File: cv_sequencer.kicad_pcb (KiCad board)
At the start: 4 copper layers, 111.3 x 22.4 mm, 106 parts, among them J1 :MIDI_IO, J10 PJ398SM, J11 PJ398SM, J12 PJ398SM, J13 PJ398SM, J2 SWD, J3 3086_Connector_Eurorack_Power, J4 3096_USBC_RA_SMD, J5 CV_OFFSET, J6 PJ398SM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

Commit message: Started firmware. Didn't realize RP2040 needed external flash. But luckily found linker script that can load and execute code straight from RAM
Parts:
- U1: value 3097_TFT_Display_SPI -> 3097_TFT+SD_1.14in

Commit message: Changes from a while ago
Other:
- board text added: "Notes from testing - For REV 0.2"
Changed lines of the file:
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@@
       (connect_pads (clearance 0))
       (min_thickness 0.254)
-      (keepout (tracks not_allowed) (vias not_allowed) (pads not_allowed ) (copperpour not_allowed) (footprints not_allowed))
+      (keepout (tracks not_allowed) (vias not_allowed) (pads not_allowed) (copperpour not_allowed) (footprints not_allowed))
       (fill (thermal_gap 0.508) (thermal_bridge_width 0.508))
       (polygon
@@
       (connect_pads (clearance 0))
       (min_thickness 0.254)
-      (keepout (tracks not_allowed) (vias not_allowed) (pads not_allowed ) (copperpour not_allowed) (footprints not_allowed))
+      (keepout (tracks not_allowed) (vias not_allowed) (pads not_allowed) (copperpour not_allowed) (footprints not_allowed))
       (fill (thermal_gap 0.508) (thermal_bridge_width 0.508))
       (polygon
@@
       (connect_pads (clearance 0))
       (min_thickness 0.254)
-      (keepout (tracks not_allowed) (vias not_allowed) (pads not_allowed ) (copperpour not_allowed) (footprints not_allowed))
+      (keepout (tracks not_allowed) (vias not_allowed) (pads not_allowed) (copperpour not_allowed) (footprints not_allowed))
       (fill (thermal_gap 0.508) (thermal_bridge_width 0.508))
       (polygon
@@
       (connect_pads (clearance 0))
       (min_thickness 0.254)
-      (keepout (tracks not_allowed) (vias not_allowed) (pads not_allowed ) (copperpour not_allowed) (footprints not_allowed))
+      (keepout (tracks not_allowed) (vias not_allowed) (pads not_allowed) (copperpour not_allowed) (footprints not_allowed))
       (fill (thermal_gap 0.508) (thermal_bridge_width 0.508))
       (polygon
@@
       (connect_pads (clearance 0))
       (min_thickness 0.254)
-      (keepout (tracks not_allowed) (vias not_allowed) (pads not_allowed ) (copperpour not_allowed) (footprints not_allowed))
+      (keepout (tracks not_allowed) (vias not_allowed) (pads not_allowed) (copperpour not_allowed) (footprints not_allowed))
       (fill (thermal_gap 0.508) (thermal_bridge_width 0.508))
       (polygon
@@
       (connect_pads (clearance 0))
       (min_thickness 0.254)
-      (keepout (tracks not_allowed) (vias not_allowed) (pads not_allowed ) (copperpour not_allowed) (footprints not_allowed))
+      (keepout (tracks not_allowed) (vias not_allowed) (pads not_allowed) (copperpour not_allowed) (footprints not_allowed))
       (fill (thermal_gap 0.508) (thermal_bridge_width 0.508))
       (polygon
@@
       (connect_pads (clearance 0))
       (min_thickness 0.254)
-      (keepout (tracks not_allowed) (vias not_allowed) (pads not_allowed ) (copperpour not_allowed) (footprints not_allowed))
+      (keepout (tracks not_allowed) (vias not_allowed) (pads not_allowed) (copperpour not_allowed) (footprints not_allowed))
       (fill (thermal_gap 0.508) (thermal_bridge_width 0.508))
       (polygon
@@
       (connect_pads (clearance 0))
       (min_thickness 0.254)
-      (keepout (tracks not_allowed) (vias not_allowed) (pads not_allowed ) (copperpour not_allowed) (footprints not_allowed))
+      (keepout (tracks not_allowed) (vias not_allowed) (pads not_allowed) (copperpour not_allowed) (footprints not_allowed))
       (fill (thermal_gap 0.508) (thermal_bridge_width 0.508))
       (polygon
@@
     (fp_line (start -2.044 -1.172) (end -1.544 -1.672) (layer "B.Fab") (width 0.1))
     (fp_arc (start -0.844 1.027999) (mid -1.404147 -0.072) (end -0.844 -1.171999) (layer "B.Fab") (width 0.1))
-    (fp_arc (start 0.855999 -1.171999) (mid 1.45984 -0.072) (end 0.856 1.027999) (layer "B.Fab") (width 0.1))
+    (fp_arc (start 0.855999 -1.171999) (mid 1.459839 -0.072) (end 0.856 1.027999) (layer "B.Fab") (width 0.1))
     (pad "1" smd rect (at -2.019 1.003) (size 1.05 0.65) (layers "B.Cu" "B.Paste" "B.Mask")
       (net 2 "GND") (pinfunction "1") (pintype "passive"))
@@
     (fp_line (start -2.044 1.528) (end 2.156 1.528) (layer "B.Fab") (width 0.1))
     (fp_arc (start -0.844 1.027999) (mid -1.404147 -0.072) (end -0.844 -1.171999) (layer "B.Fab") (width 0.1))
-    (fp_arc (start 0.855999 -1.171999) (mid 1.45984 -0.072) (end 0.856 1.027999) (layer "B.Fab") (width 0.1))
+    (fp_arc (start 0.855999 -1.171999) (mid 1.459839 -0.072) (end 0.856 1.027999) (layer "B.Fab") (width 0.1))
     (pad "1" smd rect (at 2.131 1.003 180) (size 1.05 0.65) (layers "B.Cu" "B.Paste" "B.Mask")
       (net 16 "/~{RESET}") (pinfunction "1") (pintype "passive"))
@@
     (effects (font (size 1.016 1.016) (thickness 0.1524) italic) (justify mirror))
   )
+  (gr_text "Notes from testing - For REV 0.2" (at 71.12 64.008) (layer "Cmts.User")
+    (effects (font (size 1 1) (thickness 0.15)))
+  )
   (gr_text "CV Sequencer Eurorack Module\n1U, 22HP" (at 72.009 46.736) (layer "Cmts.User")
     (effects (font (size 2.032 2.032) (thickness 0.3048)))
@@
     (height -3.8608)
     (orientation 0)
-    (gr_text "4380.0000 mils" (at 162.306 60.4012) (layer "F.Fab")
+    (gr_text "111.2520 mm" (at 162.306 60.4012) (layer "F.Fab")
       (effects (font (size 1.524 1.524) (thickness 0.3048)))
     )

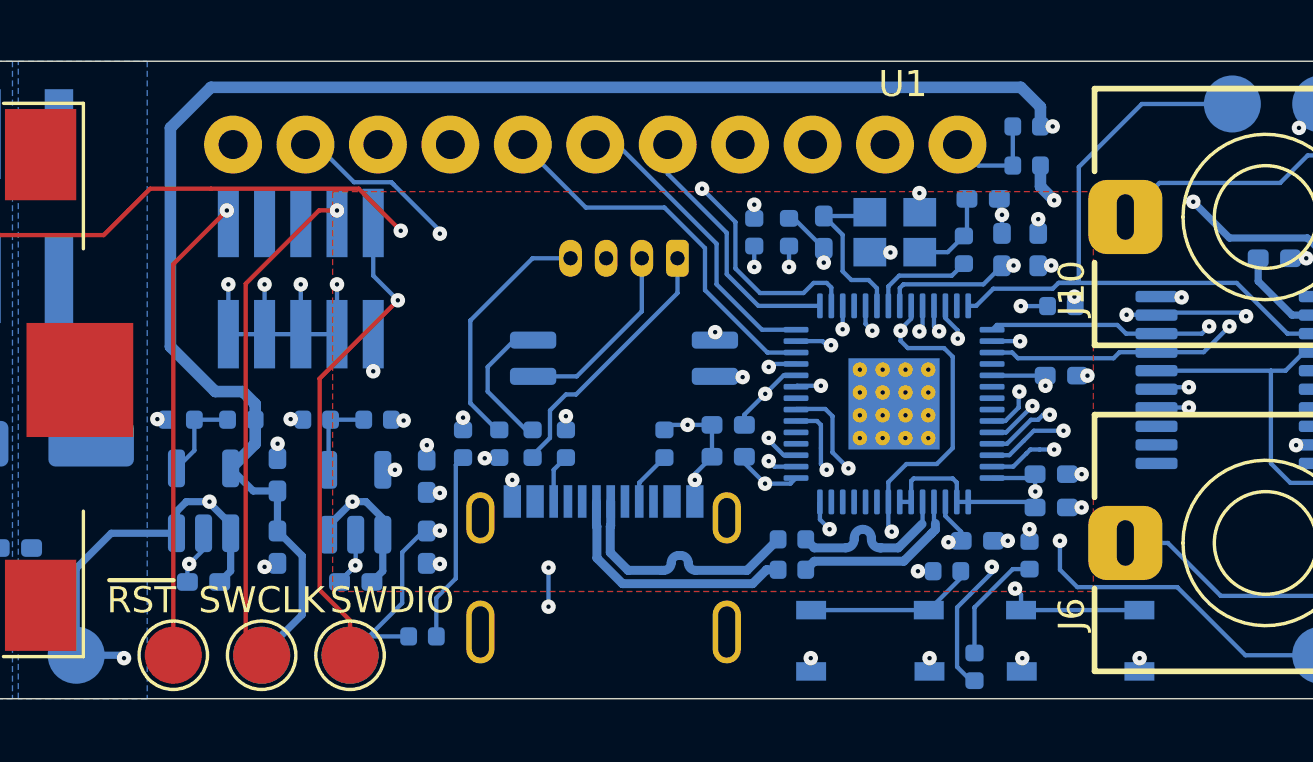
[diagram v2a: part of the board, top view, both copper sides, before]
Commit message: Routed Flash chip.. need to figure out second set of USB lines
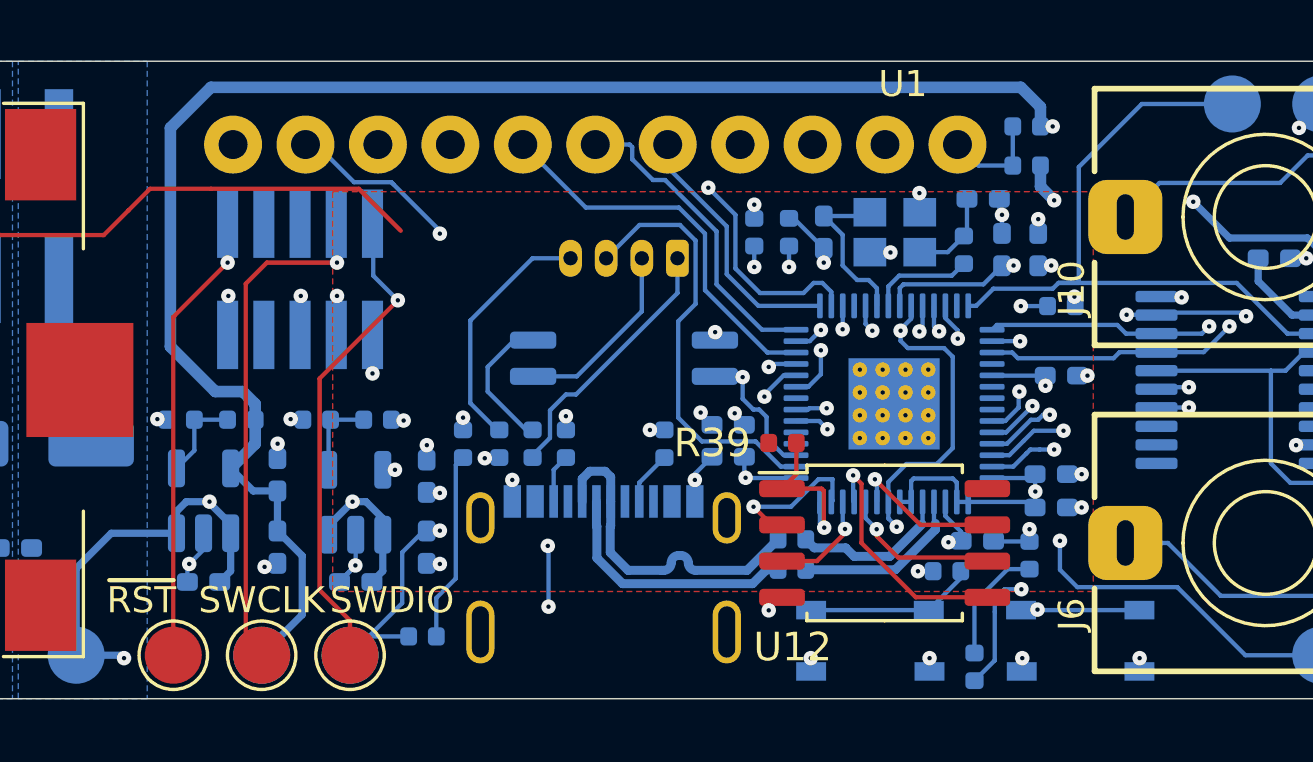
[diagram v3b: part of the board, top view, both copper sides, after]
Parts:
- added R39: 4008_Resistor_SMD_10k_0.125W_1%, Shulltronics_Generics:RES-0402, F.Cu at (146.3, 77.9)
- added U12: 4048_W25Q16JVSSIQ, Shulltronics_Integrated_Circuits:4048_16Mb_Flash_SOIC8, F.Cu at (149.9, 81.9)
- J10, J11, J12, J13, J6, J7, J8, J9: value PJ398SM -> 3085_MiniJack_Thonk_Vert
- J2: value SWD -> 4005_SWD_Header
- U1: value 3097_TFT+SD_1.14in -> 3097_TFT_Display_SPI
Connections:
- net Net-(R5-Pad1) renamed /QSPI_CS
- J2 pad 7: GND -> unconnected-(J2-Pad7)
- J4 pad B6: unconnected-(J4-PadB6) -> /USB_D+
- J4 pad B7: unconnected-(J4-PadB7) -> /USB_D-
- U2 pad 51: unconnected-(U2-Pad51) -> /QSPI_DATA3
- U2 pad 52: unconnected-(U2-Pad52) -> /QSPI_SCK
- U2 pad 53: unconnected-(U2-Pad53) -> /QSPI_DATA0
- U2 pad 54: unconnected-(U2-Pad54) -> /QSPI_DATA2
- U2 pad 55: unconnected-(U2-Pad55) -> /QSPI_DATA1
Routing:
- net GND: track 28.7 -> 16.3 mm
- net /QSPI_DATA0: track 0.00 -> 8.64 mm, vias 0 -> 1
- net /SWCLK: track 47.5 -> 41.3 mm
- net /QSPI_SCK: track 0.00 -> 5.60 mm, vias 0 -> 1
- net /QSPI_DATA3: track 0.00 -> 5.43 mm, vias 0 -> 1
- net /QSPI_DATA1: track 0.00 -> 5.24 mm, vias 0 -> 1
- net /SWDIO: track 46.0 -> 41.1 mm
- net /QSPI_CS: track 5.34 -> 10.0 mm
- net /UART_TX: track 10.5 -> 15.1 mm, vias 1 -> 0
- net /~{RESET}: track 74.4 -> 70.0 mm
- net /QSPI_DATA2: track 0.00 -> 3.74 mm, vias 0 -> 1
- net /USB_D+: track 8.94 -> 11.8 mm
- net /LCD_DC: track 21.6 -> 24.1 mm
- net /LCD/SD_SCK: track 10.7 -> 8.72 mm
- net VCC: track 59.7 -> 58.6 mm
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
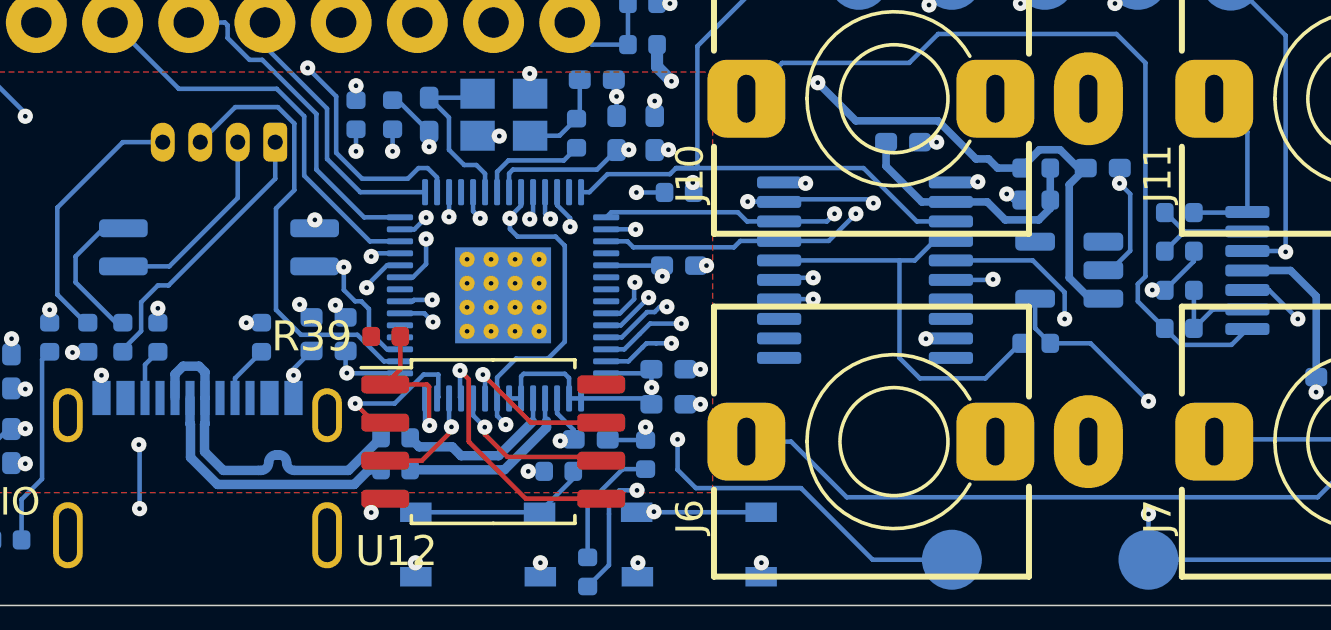
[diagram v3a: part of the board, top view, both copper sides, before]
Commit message: Added components and routed for 5v0 reference
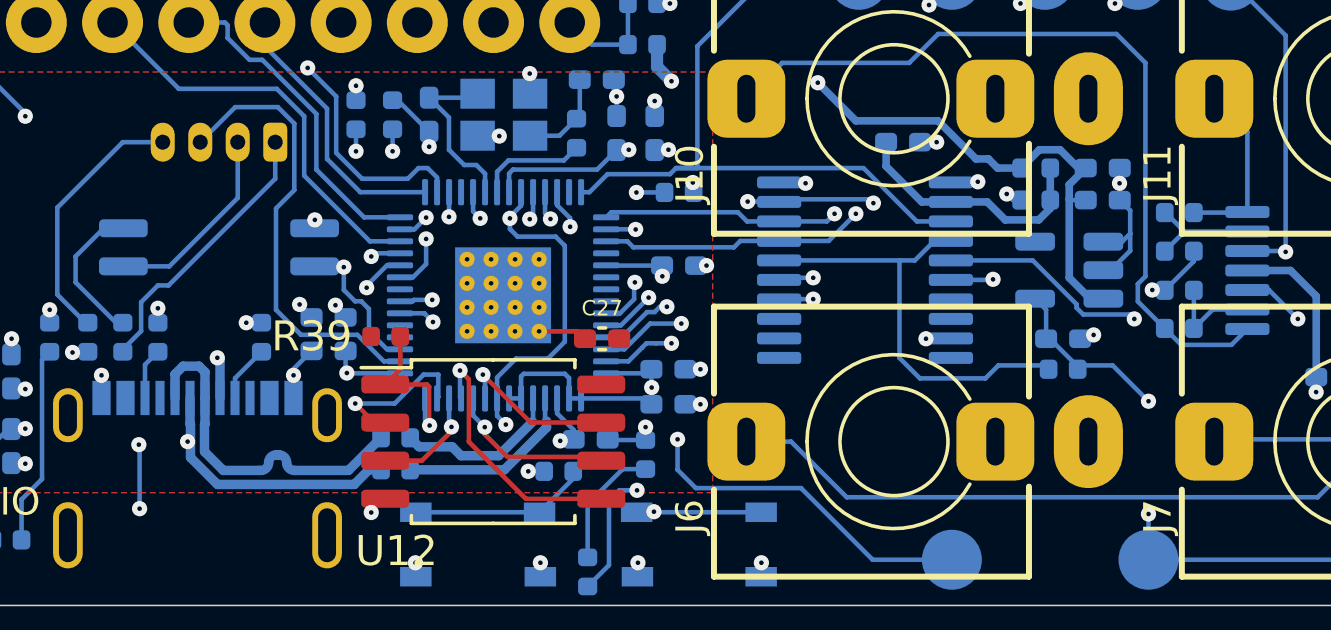
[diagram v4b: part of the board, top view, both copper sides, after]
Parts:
- added C25: 4013_Capacitor_1u_16V_0402, Shulltronics_Generics:C_0402_HandSolder, B.Cu at (170.2, 73.4)
- added C26: 4035_Capacitor_2u2_25V_0402, Shulltronics_Generics:C_0402_HandSolder, B.Cu at (168.9, 78.0)
- added C27: 3089_Capacitor_100n_16V_0402, Shulltronics_Generics:C_0402_HandSolder, F.Cu at (153.5, 78.0)
- TP10: value 5V3 -> 5V1
- TP9: value 3V1 -> 3V0
- moved R37 1.26 mm to (168.9, 79.0)
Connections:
- net /5V3 renamed /5V1
- U5 pad 1: unconnected-(U5-Pad1) -> GND
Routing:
- net /USB_D-: track 8.92 -> 13.9 mm, vias 0 -> 2
- net GND: track 16.3 -> 19.0 mm, vias 45 -> 46
- net Net-(R37-Pad2): track 14.1 -> 14.7 mm
- net /5V1: track 77.2 -> 77.8 mm
